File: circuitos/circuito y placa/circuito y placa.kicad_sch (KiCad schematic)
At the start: 2 parts, among them J1 Conn_01x03

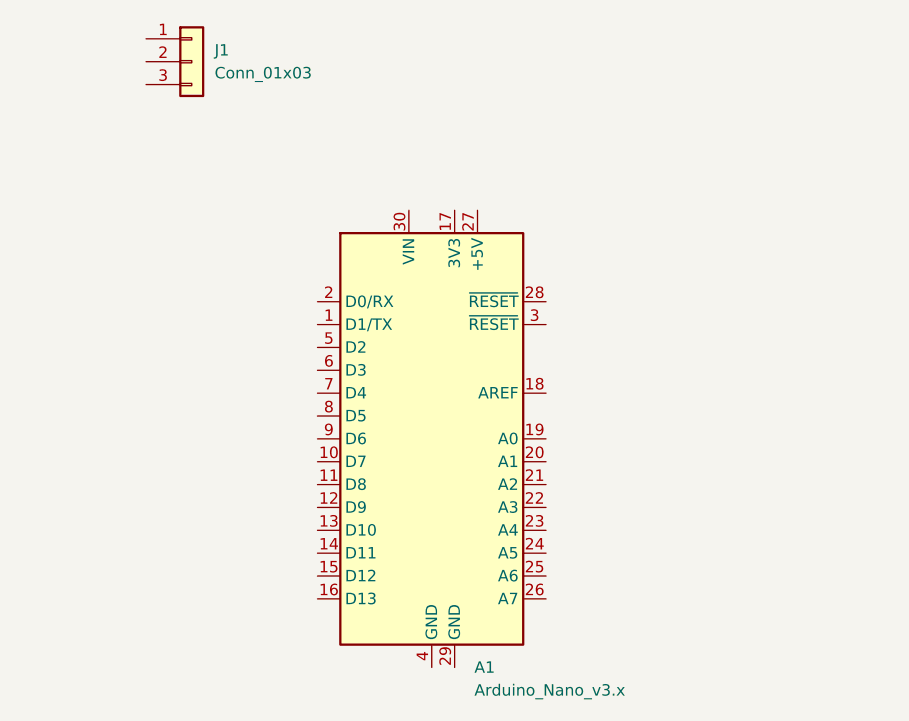
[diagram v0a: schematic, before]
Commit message: avance de diseño de placa con cambio de componentes
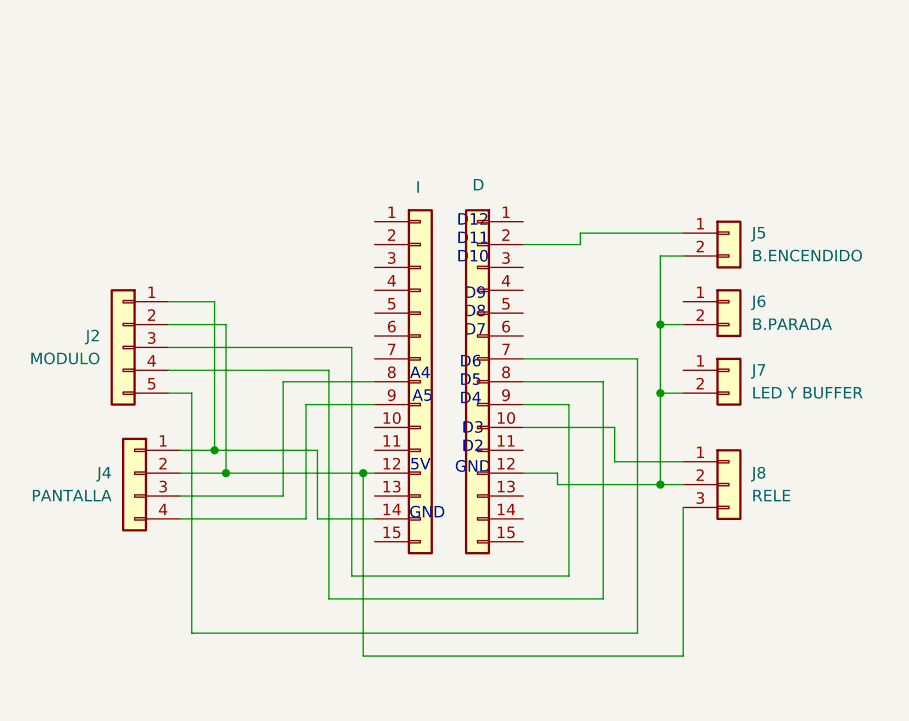
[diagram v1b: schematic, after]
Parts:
- removed A1: Arduino_Nano_v3.x, Module:Arduino_Nano, symbol MCU_Module:Arduino_Nano_v3.x
- removed J1: Conn_01x03, symbol Connector_Generic:Conn_01x03
- added D, I: ~, symbol Connector_Generic:Conn_01x15
- added J2: MODULO, symbol Connector_Generic:Conn_01x05
- added J4: PANTALLA, symbol Connector_Generic:Conn_01x04
- added J5: B.ENCENDIDO, symbol Connector_Generic:Conn_01x02
- added J6: B.PARADA, symbol Connector_Generic:Conn_01x02
- added J7: LED Y BUFFER, symbol Connector_Generic:Conn_01x02
- added J8: RELE, symbol Connector_Generic:Conn_01x03
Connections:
- new net: D.12 (Pin_12), J5.2 (Pin_2), J6.2 (Pin_2), J7.2 (Pin_2), J8.2 (Pin_2)
- new net: D.2 (Pin_2), J5.1 (Pin_1)
- new net: I.12 (Pin_12), J2.2 (Pin_2), J4.2 (Pin_2), J8.3 (Pin_3)
- new net: I.14 (Pin_14), J2.1 (Pin_1), J4.1 (Pin_1)
- new net: I.8 (Pin_8), J4.3 (Pin_3)
- new net: I.9 (Pin_9), J4.4 (Pin_4)
- new net: D.10 (Pin_10), J8.1 (Pin_1)
- new net: D.7 (Pin_7), J2.5 (Pin_5)
- new net: D.8 (Pin_8), J2.4 (Pin_4)
- new net: D.9 (Pin_9), J2.3 (Pin_3)
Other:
- note added: "5V"
- note added: "A4"
- note added: "A5"
- note added: "D12 D11 D10"
- note added: "D3 D2"
- note added: "D6 D5 D4"
- note added: "D9 D8 D7"
- note added: "GND"
